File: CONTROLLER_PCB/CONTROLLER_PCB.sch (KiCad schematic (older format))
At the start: 0 parts

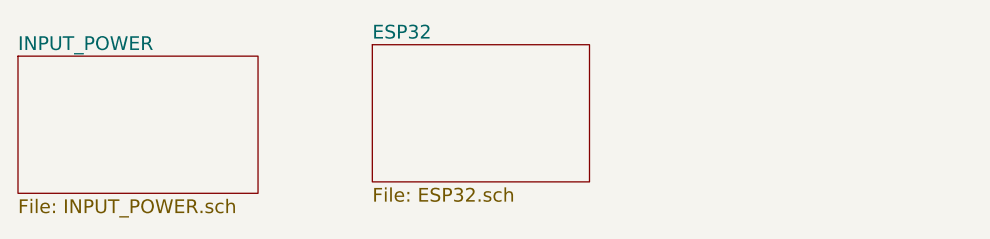
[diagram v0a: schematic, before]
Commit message: Created ESP32 pinout spreadsheet, finished MCU pinout, and added MCU_SUPPORT schematic sheet.
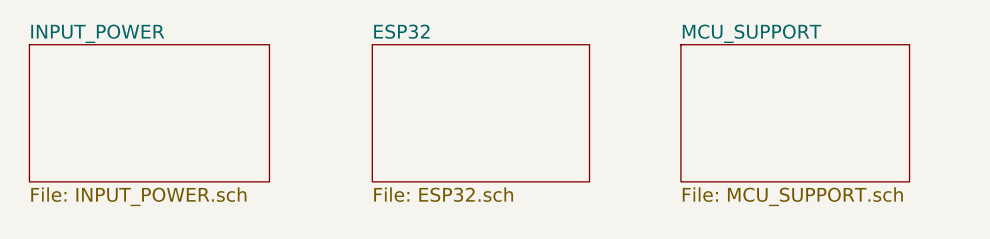
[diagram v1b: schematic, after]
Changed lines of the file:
@@
 $Descr A4 11693 8268
 encoding utf-8
-Sheet 1 3
+Sheet 1 4
 Title ""
 Date ""
@@
 $EndDescr
 $Sheet
-S 4900 3400 1050 600
+S 4950 3350 1050 600
 U 5C5A3691
 F0 "INPUT_POWER" 60
@@
 F1 "ESP32.sch" 60
 $EndSheet
+$Sheet
+S 7800 3350 1000 600
+U 5C5F103F
+F0 "MCU_SUPPORT" 60
+F1 "MCU_SUPPORT.sch" 60
+$EndSheet
 $EndSCHEMATC
